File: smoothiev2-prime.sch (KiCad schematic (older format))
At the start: 132 parts, among them J1 USB_B, J10 Conn_01x02, J15 Conn_01x02, J2 USB_A, J3 Micro_SD_Card_Det, J30 Conn_01x03_Male, J41 Conn_ARM_JTAG_SWD_10, J42 Conn_01x02, J43 Conn_01x02, J5 Screw_Terminal_01x04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

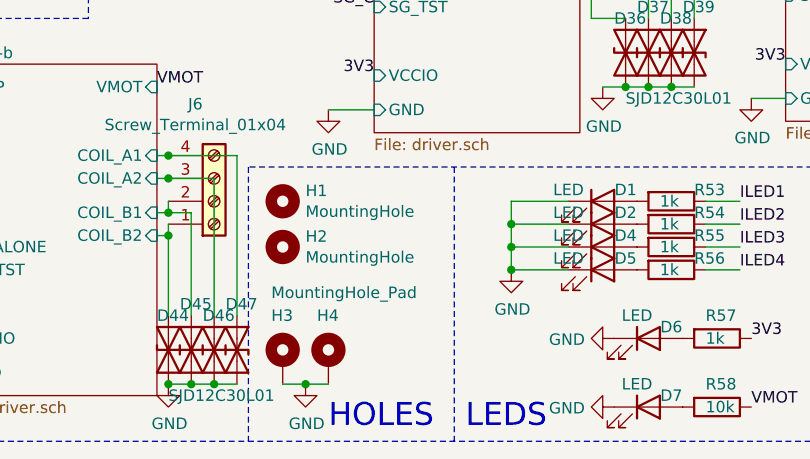
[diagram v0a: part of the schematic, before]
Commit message: Add 4x stencil8 tooling holes
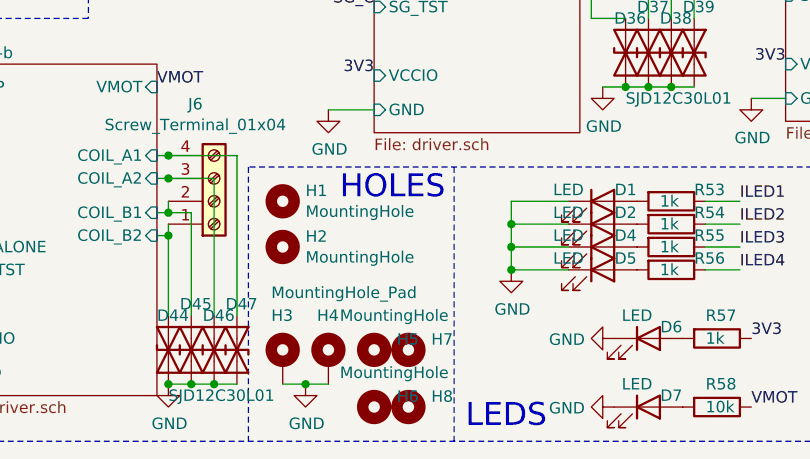
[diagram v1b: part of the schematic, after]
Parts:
- added H5, H6, H7, H8: MountingHole, smoothieparts:Stencil8_2.5mm, symbol Mechanical:MountingHole
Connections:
- net at U2.E1 (SMPS_VLX): now also C69.1, L2.2
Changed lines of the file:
@@
 Wire Notes Line
 	5350 14800 5350 16000
-Text Notes 4800 15950 0    100  ~ 0
+Text Notes 4850 14950 0    100  ~ 0
 HOLES
 Text Notes 5400 15950 0    100  ~ 0
@@
 Connection ~ 3250 6200
 Connection ~ 3250 6300
+$Comp
+L Mechanical:MountingHole H5
+U 1 1 60F05600
+P 5000 15600
+F 0 "H5" H 5100 15646 50  0000 L CNN
+F 1 "MountingHole" H 4850 15750 50  0000 L CNN
+F 2 "smoothieparts:Stencil8_2.5mm" H 5000 15600 50  0001 C CNN
+F 3 "~" H 5000 15600 50  0001 C CNN
+	1    5000 15600
+	1    0    0    -1
+$EndComp
+$Comp
+L Mechanical:MountingHole H6
+U 1 1 60F0C77D
+P 5000 15850
+F 0 "H6" H 5100 15896 50  0000 L CNN
+F 1 "MountingHole" H 4850 16000 50  0000 L CNN
+F 2 "smoothieparts:Stencil8_2.5mm" H 5000 15850 50  0001 C CNN
+F 3 "~" H 5000 15850 50  0001 C CNN
+	1    5000 15850
+	1    0    0    -1
+$EndComp
+$Comp
+L Mechanical:MountingHole H7
+U 1 1 60F13786
+P 5150 15600
+F 0 "H7" H 5250 15646 50  0000 L CNN
+F 1 "MountingHole" H 5000 15750 50  0001 L CNN
+F 2 "smoothieparts:Stencil8_2.5mm" H 5150 15600 50  0001 C CNN
+F 3 "~" H 5150 15600 50  0001 C CNN
+	1    5150 15600
+	1    0    0    -1
+$EndComp
+$Comp
+L Mechanical:MountingHole H8
+U 1 1 60F13C20
+P 5150 15850
+F 0 "H8" H 5250 15896 50  0000 L CNN
+F 1 "MountingHole" H 5000 16000 50  0001 L CNN
+F 2 "smoothieparts:Stencil8_2.5mm" H 5150 15850 50  0001 C CNN
+F 3 "~" H 5150 15850 50  0001 C CNN
+	1    5150 15850
+	1    0    0    -1
+$EndComp
 $EndSCHEMATC

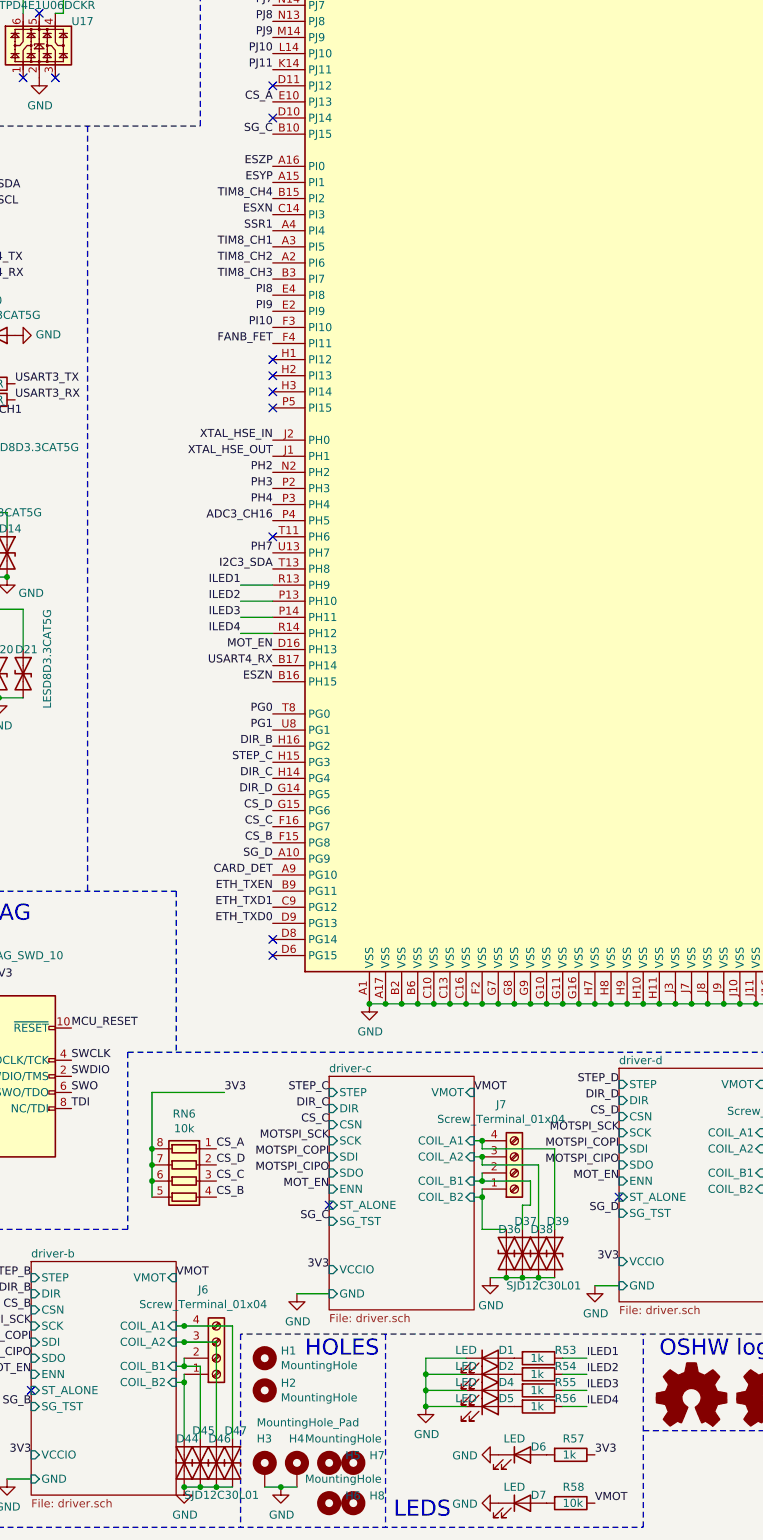
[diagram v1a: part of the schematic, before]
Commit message: Connect BOOT0 to PJ14 via 10k resistor and add indicator LED next to BOOT0 button on PF11
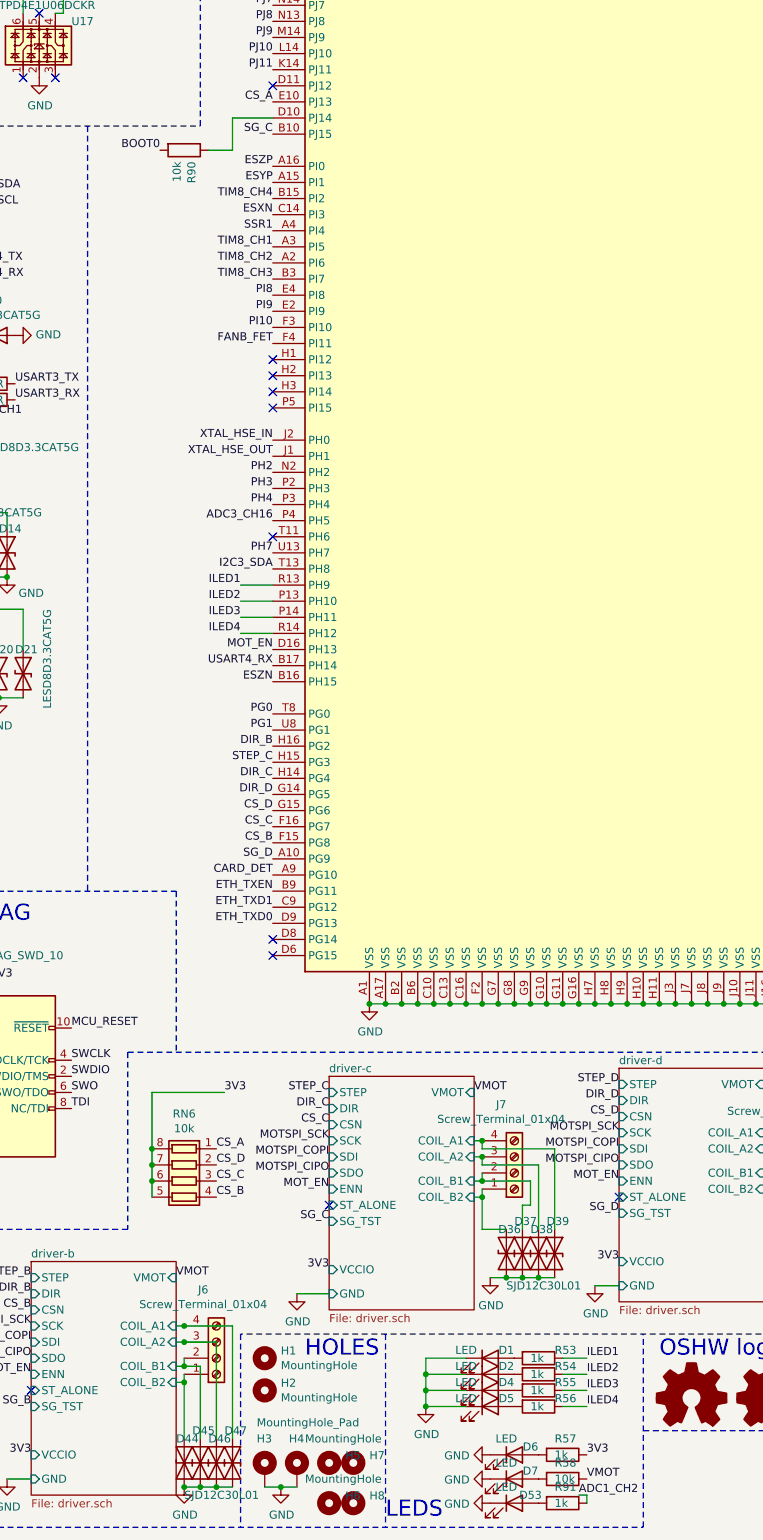
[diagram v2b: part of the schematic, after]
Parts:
- added D53: LED, LED_SMD:LED_0603_1608Metric, symbol Device:LED
- added R90: 10k, Resistor_SMD:R_0402_1005Metric, symbol Device:R
- added R91: 1k, Resistor_SMD:R_0402_1005Metric, symbol Device:R
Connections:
- net ADC1_CH2: now also R91.1
- net BOOT0: now also R90.2
- net GND: now also D53.1 (K)
- net at U2.D10 (PJ14): now also R90.1
- net at U2.E1 (SMPS_VLX): now also C69.1, L2.2
- new net: D53.2 (A), R91.2
- no-connect marks 39 -> 38
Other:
- moved on the sheet: D6, D7, R57, R58
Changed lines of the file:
@@
 L Device:R R57
 U 1 1 630E4165
-P 6500 15550
-F 0 "R57" V 6400 15500 50  0000 L CNN
-F 1 "1k" V 6500 15500 50  0000 L CNN
-F 2 "Resistor_SMD:R_0402_1005Metric" V 6430 15550 50  0001 C CNN
-F 3 "~" H 6500 15550 50  0001 C CNN
-	1    6500 15550
+P 6450 15550
+F 0 "R57" V 6350 15500 50  0000 L CNN
+F 1 "1k" V 6450 15500 50  0000 L CNN
+F 2 "Resistor_SMD:R_0402_1005Metric" V 6380 15550 50  0001 C CNN
+F 3 "~" H 6450 15550 50  0001 C CNN
+	1    6450 15550
 	0    1    1    0
 $EndComp
@@
 L Device:LED D6
 U 1 1 630E52F9
-P 6200 15550
-F 0 "D6" H 6300 15600 50  0000 C CNN
-F 1 "LED" H 6150 15650 50  0000 C CNN
-F 2 "LED_SMD:LED_0603_1608Metric" H 6200 15550 50  0001 C CNN
-F 3 "~" H 6200 15550 50  0001 C CNN
-	1    6200 15550
+P 6150 15550
+F 0 "D6" H 6250 15600 50  0000 C CNN
+F 1 "LED" H 6100 15650 50  0000 C CNN
+F 2 "LED_SMD:LED_0603_1608Metric" H 6150 15550 50  0001 C CNN
+F 3 "~" H 6150 15550 50  0001 C CNN
+	1    6150 15550
 	1    0    0    -1
 $EndComp
@@
 L power:GND #PWR0139
 U 1 1 630E6C8D
-P 6050 15550
+P 6000 15550
 AR Path="/630E6C8D" Ref="#PWR0139"  Part="1"
 AR Path="/60D8BE45/630E6C8D" Ref="#PWR?"  Part="1"
-F 0 "#PWR0139" H 6050 15300 50  0001 C CNN
-F 1 "GND" V 6055 15422 50  0000 R CNN
-F 2 "" H 6050 15550 50  0001 C CNN
-F 3 "" H 6050 15550 50  0001 C CNN
-	1    6050 15550
-	0    1    1    0
-$EndComp
-Text Label 6650 15550 0    50   ~ 0
+F 0 "#PWR0139" H 6000 15300 50  0001 C CNN
+F 1 "GND" V 6005 15422 50  0000 R CNN
+F 2 "" H 6000 15550 50  0001 C CNN
+F 3 "" H 6000 15550 50  0001 C CNN
+	1    6000 15550
+	0    1    1    0
+$EndComp
+Text Label 6600 15550 0    50   ~ 0
 3V3
 $Comp
 L Device:R R58
 U 1 1 630F9C34
-P 6500 15850
-F 0 "R58" V 6400 15800 50  0000 L CNN
-F 1 "10k" V 6500 15800 50  0000 L CNN
-F 2 "Resistor_SMD:R_0402_1005Metric" V 6430 15850 50  0001 C CNN
-F 3 "~" H 6500 15850 50  0001 C CNN
-	1    6500 15850
+P 6450 15700
+F 0 "R58" V 6350 15650 50  0000 L CNN
+F 1 "10k" V 6450 15650 50  0000 L CNN
+F 2 "Resistor_SMD:R_0402_1005Metric" V 6380 15700 50  0001 C CNN
+F 3 "~" H 6450 15700 50  0001 C CNN
+	1    6450 15700
 	0    1    1    0
 $EndComp
@@
 L Device:LED D7
 U 1 1 630F9F1C
-P 6200 15850
-F 0 "D7" H 6300 15900 50  0000 C CNN
-F 1 "LED" H 6150 15950 50  0000 C CNN
-F 2 "LED_SMD:LED_0603_1608Metric" H 6200 15850 50  0001 C CNN
-F 3 "~" H 6200 15850 50  0001 C CNN
-	1    6200 15850
+P 6150 15700
+F 0 "D7" H 6250 15750 50  0000 C CNN
+F 1 "LED" H 6100 15800 50  0000 C CNN
+F 2 "LED_SMD:LED_0603_1608Metric" H 6150 15700 50  0001 C CNN
+F 3 "~" H 6150 15700 50  0001 C CNN
+	1    6150 15700
 	1    0    0    -1
 $EndComp
@@
 L power:GND #PWR041
 U 1 1 630F9F26
-P 6050 15850
+P 6000 15700
 AR Path="/630F9F26" Ref="#PWR041"  Part="1"
 AR Path="/60D8BE45/630F9F26" Ref="#PWR?"  Part="1"
-F 0 "#PWR041" H 6050 15600 50  0001 C CNN
-F 1 "GND" V 6055 15722 50  0000 R CNN
-F 2 "" H 6050 15850 50  0001 C CNN
-F 3 "" H 6050 15850 50  0001 C CNN
-	1    6050 15850
-	0    1    1    0
-$EndComp
-Text Label 6650 15850 0    50   ~ 0
+F 0 "#PWR041" H 6000 15450 50  0001 C CNN
+F 1 "GND" V 6005 15572 50  0000 R CNN
+F 2 "" H 6000 15700 50  0001 C CNN
+F 3 "" H 6000 15700 50  0001 C CNN
+	1    6000 15700
+	0    1    1    0
+$EndComp
+Text Label 6600 15700 0    50   ~ 0
 VMOT
 Text Label 1800 13950 0    50   ~ 0
@@
 NoConn ~ 4650 6350
 NoConn ~ 4650 7050
-NoConn ~ 4650 7250
 NoConn ~ 4650 8750
 NoConn ~ 4650 8850
@@
 Text Notes 4850 14950 0    100  ~ 0
 HOLES
-Text Notes 5400 15950 0    100  ~ 0
+Text Notes 5350 15950 0    100  ~ 0
 LEDS
 Wire Notes Line
@@
 	1    0    0    -1
 $EndComp
+Text Label 3950 7450 2    50   ~ 0
+BOOT0
+$Comp
+L Device:R R90
+U 1 1 610FB4D1
+P 4100 7450
+F 0 "R90" H 4170 7496 50  0000 L CNN
+F 1 "10k" H 4170 7405 50  0000 L CNN
+F 2 "Resistor_SMD:R_0402_1005Metric" V 4030 7450 50  0001 C CNN
+F 3 "~" H 4100 7450 50  0001 C CNN
+	1    4100 7450
+	0    1    1    0
+$EndComp
+Wire Wire Line
+	4650 7250 4400 7250
+Wire Wire Line
+	4400 7250 4400 7450
+Wire Wire Line
+	4400 7450 4250 7450
+$Comp
+L Device:R R91
+U 1 1 61195070
+P 6450 15850
+F 0 "R91" V 6350 15800 50  0000 L CNN
+F 1 "1k" V 6450 15800 50  0000 L CNN
+F 2 "Resistor_SMD:R_0402_1005Metric" V 6380 15850 50  0001 C CNN
+F 3 "~" H 6450 15850 50  0001 C CNN
+	1    6450 15850
+	0    1    1    0
+$EndComp
+$Comp
+L Device:LED D53
+U 1 1 611952D2
+P 6150 15850
+F 0 "D53" H 6250 15900 50  0000 C CNN
+F 1 "LED" H 6100 15950 50  0000 C CNN
+F 2 "LED_SMD:LED_0603_1608Metric" H 6150 15850 50  0001 C CNN
+F 3 "~" H 6150 15850 50  0001 C CNN
+	1    6150 15850
+	1    0    0    -1
+$EndComp
+$Comp
+L power:GND #PWR072
+U 1 1 611952DC
+P 6000 15850
+AR Path="/611952DC" Ref="#PWR072"  Part="1"
+AR Path="/60D8BE45/611952DC" Ref="#PWR?"  Part="1"
+F 0 "#PWR072" H 6000 15600 50  0001 C CNN
+F 1 "GND" V 6005 15722 50  0000 R CNN
+F 2 "" H 6000 15850 50  0001 C CNN
+F 3 "" H 6000 15850 50  0001 C CNN
+	1    6000 15850
+	0    1    1    0
+$EndComp
+Text Label 6550 15800 0    50   ~ 0
+ADC1_CH2
+Wire Wire Line
+	6550 15800 6600 15800
+Wire Wire Line
+	6600 15800 6600 15850
 $EndSCHEMATC

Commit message: Rearrange ADC channels to place all thermistors on ADC1 and expose more ADC1 channels on expansion headers.
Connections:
- net FETSENSE: now also U2.K4 (PF8); no longer U2.M4 (PC3)
- net T3: now also U2.U5 (PB0); no longer U2.P7 (PF13)
- net T4: now also U2.T7 (PF11); no longer U2.U5 (PB0)
- net VMOTSENSE: now also U2.P4 (PH5); no longer U2.U2 (PA3)
- net at U2.E1 (SMPS_VLX): now also C69.1, L2.2
- net ADC1_CH2 renamed PF13
- net PF13: now also U2.P7 (PF13); no longer U2.T7 (PF11)
- net ADC3_CH16 renamed ADC1_CH13
- net ADC1_CH13: now also U2.M4 (PC3); no longer U2.P4 (PH5)
- net ADC3_CH7 renamed ADC1_CH15
- net ADC1_CH15: now also U2.U2 (PA3); no longer U2.K4 (PF8)
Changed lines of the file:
@@
 Text Label 10450 12150 0    50   ~ 0
 T2
-Text Label 10450 12250 0    50   ~ 0
+Text Label 10450 4150 0    50   ~ 0
 T3
 Text Label 1550 8450 2    50   ~ 0
@@
 Text Label 10450 11950 0    50   ~ 0
 ADC3_CH6
-Text Label 10450 11750 0    50   ~ 0
-ADC3_CH7
 Text Label 10450 11550 0    50   ~ 0
 ADC3_CH8
 Text Label 10450 11350 0    50   ~ 0
 ADC3_CH9
-Text Label 10450 4150 0    50   ~ 0
+Text Label 10450 12050 0    50   ~ 0
 T4
 Text Label 10450 6050 0    50   ~ 0
 ADC1_CH12
-Text Label 10450 2750 0    50   ~ 0
+Text Label 4650 9750 2    50   ~ 0
 VMOTSENSE
 Text Label 1150 15050 2    50   ~ 0
@@
 Text Label 1550 10300 2    50   ~ 0
 PH2
-Text Label 4650 9750 2    50   ~ 0
-ADC3_CH16
 Text Label 10450 5850 0    50   ~ 0
 PC0
@@
 Text Label 10450 11150 0    50   ~ 0
 PF2
-Text Label 2250 10400 0    50   ~ 0
-ADC3_CH7
 Text Label 2250 10500 0    50   ~ 0
 ADC1_CH12
-Text Label 2250 10300 0    50   ~ 0
-ADC3_CH16
 Text Label 10450 7150 0    50   ~ 0
 PC13
@@
 Text Label 5250 1050 2    50   ~ 0
 VMOTSENSE
-Text Label 10450 6150 0    50   ~ 0
+Text Label 10450 11750 0    50   ~ 0
 FETSENSE
 Text Label 10400 14600 2    50   ~ 0
@@
 	1    0    0    -1
 $EndComp
-Text Label 10450 12050 0    50   ~ 0
-ADC1_CH2
 $Comp
 L Device:R_Pack04 RN?
@@
 	0    1    1    0
 $EndComp
-Text Label 6550 15800 0    50   ~ 0
-ADC1_CH2
-Wire Wire Line
-	6550 15800 6600 15800
-Wire Wire Line
-	6600 15800 6600 15850
+Text Label 10450 2750 0    50   ~ 0
+ADC1_CH15
+Text Label 2250 10400 0    50   ~ 0
+ADC1_CH15
+Text Label 10450 6150 0    50   ~ 0
+ADC1_CH13
+Text Label 2250 10300 0    50   ~ 0
+ADC1_CH13
+Text Label 10450 12250 0    50   ~ 0
+PF13
+Text Label 6600 15850 0    50   ~ 0
+PF13
 $EndSCHEMATC

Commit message: Fix FPs for U4 and U9
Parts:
- U4: footprint Package_SO:SOIC-8_3.9x4.9mm_P1.27mm -> Package_SO:SOIC-8_5.23x5.23mm_P1.27mm
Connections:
- net at U2.E1 (SMPS_VLX): now also C69.1, L2.2
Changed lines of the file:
@@
 F 0 "U4" H 1850 6500 50  0000 L CNN
 F 1 "AT25SF081-SSHF-X" H 750 6500 50  0000 L CNN
-F 2 "Package_SO:SOIC-8_3.9x4.9mm_P1.27mm" H 1600 5450 50  0001 C CNN
+F 2 "Package_SO:SOIC-8_5.23x5.23mm_P1.27mm" H 1600 5450 50  0001 C CNN
 F 3 "https://www.adestotech.com/wp-content/uploads/DS-AT25SF081_045.pdf" H 1600 6050 50  0001 C CNN
 	1    1600 6050

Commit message: Fix flipped motor MOSFETS. Add reverse current block and current limit to 5V DC/DC supply. Add pullups to SD and card detect.
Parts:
- added R94, R95: 10k, Resistor_SMD:R_0402_1005Metric, symbol Device:R
- added RN7: 10k, Resistor_SMD:R_Array_Concave_4x0603, symbol Device:R_Pack04
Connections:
- net 3V3: now also R94.2, R95.2, RN7.1 (R1.1), RN7.2 (R2.1), RN7.3 (R3.1), RN7.4 (R4.1)
- net CARD_DET: now also R94.1
- net SD_CMD: now also RN7.7 (R2.2)
- net SD_D0: now also RN7.8 (R1.2)
- net SD_D1: now also R95.1
- net SD_D2: now also RN7.6 (R3.2)
- net SD_D3: now also RN7.5 (R4.2)
- net at U2.E1 (SMPS_VLX): now also C69.1, L2.2
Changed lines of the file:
@@
 NoConn ~ 10450 3450
 NoConn ~ 10450 4550
-NoConn ~ 10450 2450
 NoConn ~ 10450 6550
 NoConn ~ 10450 7650
@@
 Text Label 6600 15850 0    50   ~ 0
 PF13
+$Comp
+L Device:R_Pack04 RN?
+U 1 1 615C7304
+P 2950 1200
+AR Path="/612538A5/615C7304" Ref="RN?"  Part="1"
+AR Path="/615C7304" Ref="RN7"  Part="1"
+F 0 "RN7" V 2533 1200 50  0000 C CNN
+F 1 "10k" V 2624 1200 50  0000 C CNN
+F 2 "Resistor_SMD:R_Array_Concave_4x0603" V 3225 1200 50  0001 C CNN
+F 3 "~" H 2950 1200 50  0001 C CNN
+	1    2950 1200
+	0    -1   1    0
+$EndComp
+Wire Wire Line
+	2250 1150 2550 1150
+Wire Wire Line
+	2550 1150 2550 1000
+Wire Wire Line
+	2550 1000 2750 1000
+Wire Wire Line
+	2250 1550 2600 1550
+Wire Wire Line
+	2600 1550 2600 1100
+Wire Wire Line
+	2600 1100 2750 1100
+Text Label 2750 1300 2    50   ~ 0
+SD_D3
+Text Label 2750 1200 2    50   ~ 0
+SD_D2
+Wire Wire Line
+	2700 1450 3150 1450
+Wire Wire Line
+	3150 1450 3150 1300
+Connection ~ 2700 1450
+Connection ~ 3150 1100
+Wire Wire Line
+	3150 1100 3150 1000
+Connection ~ 3150 1200
+Wire Wire Line
+	3150 1200 3150 1100
+Connection ~ 3150 1300
+Wire Wire Line
+	3150 1300 3150 1200
+$Comp
+L Device:R R95
+U 1 1 616855B4
+P 2650 900
+F 0 "R95" H 2580 854 50  0000 R CNN
+F 1 "10k" H 2580 945 50  0000 R CNN
+F 2 "Resistor_SMD:R_0402_1005Metric" V 2580 900 50  0001 C CNN
+F 3 "~" H 2650 900 50  0001 C CNN
+	1    2650 900
+	0    -1   1    0
+$EndComp
+Wire Wire Line
+	2800 900  3150 900
+Wire Wire Line
+	3150 900  3150 1000
+Connection ~ 3150 1000
+Wire Wire Line
+	2250 1050 2500 1050
+Wire Wire Line
+	2500 1050 2500 900
+$Comp
+L Device:R R94
+U 1 1 616FE89A
+P 2400 700
+F 0 "R94" H 2330 654 50  0000 R CNN
+F 1 "10k" H 2330 745 50  0000 R CNN
+F 2 "Resistor_SMD:R_0402_1005Metric" V 2330 700 50  0001 C CNN
+F 3 "~" H 2400 700 50  0001 C CNN
+	1    2400 700
+	0    -1   1    0
+$EndComp
+Wire Wire Line
+	2550 700  2800 700
+Wire Wire Line
+	2800 700  2800 900
+Connection ~ 2800 900
+Wire Wire Line
+	2250 700  2250 850
+NoConn ~ 10450 2450
 $EndSCHEMATC

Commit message: Switch ADC opamp to 5V Add 4.7k series resistors (RN9) to thermistor inputs. Add 10k pulldowns (RN8) to FET gate driver inputs.
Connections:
- net at U2.E1 (SMPS_VLX): now also C69.1, L2.2
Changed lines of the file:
@@
 F16 "5V_LIMIT_IN" I L 1150 12500 50
 F17 "3V3_LIMIT_IN" I L 1150 12600 50
+F18 "5V_IN" I L 1150 12800 50
 $EndSheet
 Text Label 3250 6100 0    50   ~ 0
@@
 	2250 700  2250 850
 NoConn ~ 10450 2450
+Text Label 1050 12800 2    50   ~ 0
+5V
+Wire Wire Line
+	1050 12800 1150 12800
 $EndSCHEMATC
